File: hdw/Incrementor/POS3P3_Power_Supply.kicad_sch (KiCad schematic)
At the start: 13 parts, among them U301 TPS62130

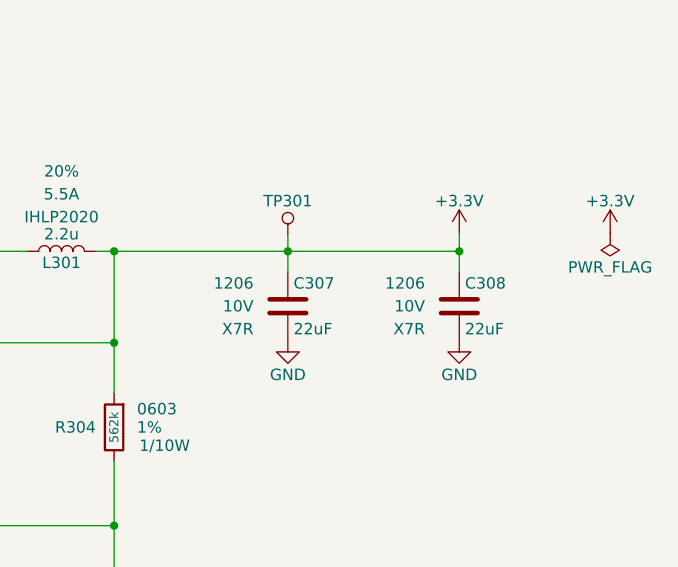
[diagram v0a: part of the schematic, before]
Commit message: renamed project, removed stuff I dont need
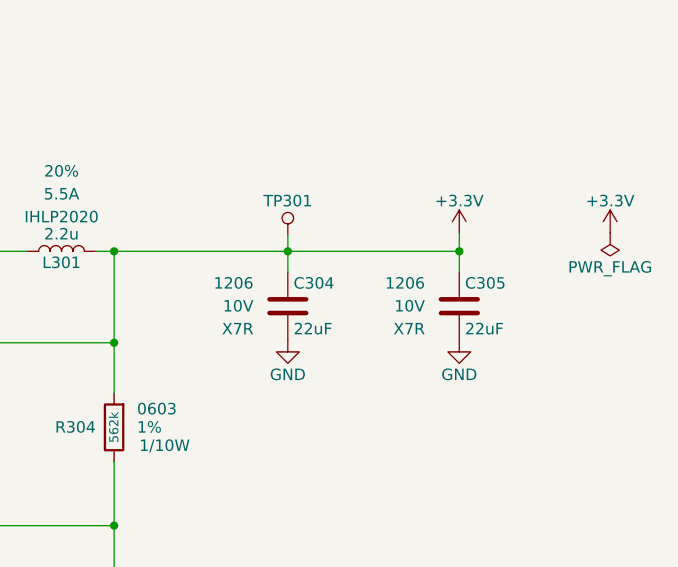
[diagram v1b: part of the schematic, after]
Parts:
- renumbered C307 to C304, C308 to C305
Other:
- company: (none) -> Drew Maatman
- title: QI Charger -> Stopwatch
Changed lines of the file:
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@@
   (paper "A")
   (title_block
-    (title "QI Charger")
-    (date "2019-01-03")
+    (title "Stopwatch")
+    (date "2024-01-02")
     (rev "A")
+    (company "Drew Maatman")
   )
   (junction (at 63.5 93.726) (diameter 0) (color 0 0 0 0)
@@
     (pin "2")
     (instances
-      (project "Incrementor"
+      (project "Stopwatch"
         (path "/c0d2575b-aec2-49ed-8c32-97fe6e68824c/00000000-0000-0000-0000-00005d779ae1"
           (reference "L301") (unit 1)
@@
   (symbol (lib_id "Custom_Library:C_Custom") (at 108.712 61.468 0) (unit 1)
     (in_bom yes) (on_board yes) (dnp no)
-    (property "Reference" "C?" (at 109.347 58.928 0)
+    (property "Reference" "C303" (at 109.347 58.928 0)
       (effects (font (size 1.27 1.27)) (justify left))
     )
@@
     (pin "2")
     (instances
-      (project "Incrementor"
+      (project "Stopwatch"
         (path "/c0d2575b-aec2-49ed-8c32-97fe6e68824c/00000000-0000-0000-0000-00005d779ae1"
           (reference "C303") (unit 1)
@@
     )
     (pin "1")
+    (instances
+      (project "Stopwatch"
+        (path "/c0d2575b-aec2-49ed-8c32-97fe6e68824c/00000000-0000-0000-0000-00005d779ae1"
+          (reference "#PWR0305") (unit 1)
+        )
+      )
+    )
   )
   (symbol (lib_id "Custom_Library:C_Custom") (at 63.5 61.468 0) (unit 1)
@@
     (pin "2")
     (instances
-      (project "Incrementor"
+      (project "Stopwatch"
         (path "/c0d2575b-aec2-49ed-8c32-97fe6e68824c/00000000-0000-0000-0000-00005d779ae1"
           (reference "C301") (unit 1)
@@
     )
     (pin "1")
+    (instances
+      (project "Stopwatch"
+        (path "/c0d2575b-aec2-49ed-8c32-97fe6e68824c/00000000-0000-0000-0000-00005d779ae1"
+          (reference "#PWR0302") (unit 1)
+        )
+      )
+    )
   )
   (symbol (lib_id "power:+12V") (at 63.5 51.054 0) (unit 1)
@@
     )
     (pin "1")
+    (instances
+      (project "Stopwatch"
+        (path "/c0d2575b-aec2-49ed-8c32-97fe6e68824c/00000000-0000-0000-0000-00005d779ae1"
+          (reference "#PWR0301") (unit 1)
+        )
+      )
+    )
   )
   (symbol (lib_id "Custom_Library:TPS62130") (at 130.048 81.026 0) (unit 1)
@@
     (pin "9")
     (instances
-      (project "Incrementor"
+      (project "Stopwatch"
         (path "/c0d2575b-aec2-49ed-8c32-97fe6e68824c/00000000-0000-0000-0000-00005d779ae1"
           (reference "U301") (unit 1)
@@
   (symbol (lib_id "Custom_Library:R_Custom") (at 86.36 61.468 0) (unit 1)
     (in_bom yes) (on_board yes) (dnp no)
-    (property "Reference" "R?" (at 84.328 61.468 0)
+    (property "Reference" "R302" (at 84.328 61.468 0)
       (effects (font (size 1.27 1.27)) (justify right))
     )
@@
     (pin "2")
     (instances
-      (project "Incrementor"
+      (project "Stopwatch"
         (path "/c0d2575b-aec2-49ed-8c32-97fe6e68824c/00000000-0000-0000-0000-00005d779ae1"
           (reference "R302") (unit 1)
@@
     )
     (pin "1")
+    (instances
+      (project "Stopwatch"
+        (path "/c0d2575b-aec2-49ed-8c32-97fe6e68824c/00000000-0000-0000-0000-00005d779ae1"
+          (reference "#PWR0303") (unit 1)
+        )
+      )
+    )
   )
   (symbol (lib_id "power:GND") (at 130.048 116.078 0) (unit 1)
@@
     )
     (pin "1")
+    (instances
+      (project "Stopwatch"
+        (path "/c0d2575b-aec2-49ed-8c32-97fe6e68824c/00000000-0000-0000-0000-00005d779ae1"
+          (reference "#PWR0307") (unit 1)
+        )
+      )
+    )
   )
   (symbol (lib_id "power:GND") (at 115.316 110.998 0) (unit 1)
@@
     )
     (pin "1")
+    (instances
+      (project "Stopwatch"
+        (path "/c0d2575b-aec2-49ed-8c32-97fe6e68824c/00000000-0000-0000-0000-00005d779ae1"
+          (reference "#PWR0306") (unit 1)
+        )
+      )
+    )
   )
   (symbol (lib_id "Custom_Library:C_Custom") (at 179.07 69.342 0) (unit 1)
     (in_bom yes) (on_board yes) (dnp no)
-    (property "Reference" "C307" (at 179.705 66.802 0)
+    (property "Reference" "C304" (at 179.705 66.802 0)
       (effects (font (size 1.27 1.27)) (justify left))
     )
@@
     (pin "2")
     (instances
-      (project "Incrementor"
+      (project "Stopwatch"
         (path "/c0d2575b-aec2-49ed-8c32-97fe6e68824c/00000000-0000-0000-0000-00005d779ae1"
           (reference "C304") (unit 1)
@@
   (symbol (lib_id "Custom_Library:R_Custom") (at 63.5 82.804 0) (unit 1)
     (in_bom yes) (on_board yes) (dnp no)
-    (property "Reference" "R?" (at 61.468 82.804 0)
+    (property "Reference" "R301" (at 61.468 82.804 0)
       (effects (font (size 1.27 1.27)) (justify right))
     )
@@
     (pin "2")
     (instances
-      (project "Incrementor"
+      (project "Stopwatch"
         (path "/c0d2575b-aec2-49ed-8c32-97fe6e68824c/00000000-0000-0000-0000-00005d779ae1"
           (reference "R301") (unit 1)
@@
   (symbol (lib_id "Custom_Library:C_Custom") (at 99.568 107.188 0) (unit 1)
     (in_bom yes) (on_board yes) (dnp no)
-    (property "Reference" "C?" (at 100.203 104.648 0)
+    (property "Reference" "C302" (at 100.203 104.648 0)
       (effects (font (size 1.27 1.27)) (justify left))
     )
@@
     (pin "2")
     (instances
-      (project "Incrementor"
+      (project "Stopwatch"
         (path "/c0d2575b-aec2-49ed-8c32-97fe6e68824c/00000000-0000-0000-0000-00005d779ae1"
           (reference "C302") (unit 1)
@@
     )
     (pin "1")
+    (instances
+      (project "Stopwatch"
+        (path "/c0d2575b-aec2-49ed-8c32-97fe6e68824c/00000000-0000-0000-0000-00005d779ae1"
+          (reference "#PWR0304") (unit 1)
+        )
+      )
+    )
   )
   (symbol (lib_id "Custom_Library:R_Custom") (at 159.766 82.804 0) (unit 1)
     (in_bom yes) (on_board yes) (dnp no)
-    (property "Reference" "R?" (at 157.734 82.804 0)
+    (property "Reference" "R304" (at 157.734 82.804 0)
       (effects (font (size 1.27 1.27)) (justify right))
     )
@@
     (pin "2")
     (instances
-      (project "Incrementor"
+      (project "Stopwatch"
         (path "/c0d2575b-aec2-49ed-8c32-97fe6e68824c/00000000-0000-0000-0000-00005d779ae1"
           (reference "R304") (unit 1)
@@
   (symbol (lib_id "Custom_Library:R_Custom") (at 159.766 105.918 0) (unit 1)
     (in_bom yes) (on_board yes) (dnp no)
-    (property "Reference" "R?" (at 157.734 105.918 0)
+    (property "Reference" "R305" (at 157.734 105.918 0)
       (effects (font (size 1.27 1.27)) (justify right))
     )
@@
     (pin "2")
     (instances
-      (project "Incrementor"
+      (project "Stopwatch"
         (path "/c0d2575b-aec2-49ed-8c32-97fe6e68824c/00000000-0000-0000-0000-00005d779ae1"
           (reference "R305") (unit 1)
@@
     )
     (pin "1")
+    (instances
+      (project "Stopwatch"
+        (path "/c0d2575b-aec2-49ed-8c32-97fe6e68824c/00000000-0000-0000-0000-00005d779ae1"
+          (reference "#PWR0308") (unit 1)
+        )
+      )
+    )
   )
   (symbol (lib_id "power:GND") (at 179.07 73.152 0) (unit 1)
@@
     )
     (pin "1")
+    (instances
+      (project "Stopwatch"
+        (path "/c0d2575b-aec2-49ed-8c32-97fe6e68824c/00000000-0000-0000-0000-00005d779ae1"
+          (reference "#PWR0309") (unit 1)
+        )
+      )
+    )
   )
   (symbol (lib_id "Custom_Library:C_Custom") (at 198.12 69.342 0) (unit 1)
     (in_bom yes) (on_board yes) (dnp no)
-    (property "Reference" "C308" (at 198.755 66.802 0)
+    (property "Reference" "C305" (at 198.755 66.802 0)
       (effects (font (size 1.27 1.27)) (justify left))
     )
@@
     (pin "2")
     (instances
-      (project "Incrementor"
+      (project "Stopwatch"
         (path "/c0d2575b-aec2-49ed-8c32-97fe6e68824c/00000000-0000-0000-0000-00005d779ae1"
           (reference "C305") (unit 1)
@@
     )
     (pin "1")
+    (instances
+      (project "Stopwatch"
+        (path "/c0d2575b-aec2-49ed-8c32-97fe6e68824c/00000000-0000-0000-0000-00005d779ae1"
+          (reference "#PWR0310") (unit 1)
+        )
+      )
+    )
   )
   (symbol (lib_id "Custom_Library:R_Custom") (at 86.36 82.804 0) (unit 1)
     (in_bom yes) (on_board yes) (dnp no)
-    (property "Reference" "R?" (at 84.328 82.804 0)
+    (property "Reference" "R303" (at 84.328 82.804 0)
       (effects (font (size 1.27 1.27)) (justify right))
     )
@@
     (pin "2")
     (instances
-      (project "Incrementor"
+      (project "Stopwatch"
         (path "/c0d2575b-aec2-49ed-8c32-97fe6e68824c/00000000-0000-0000-0000-00005d779ae1"
           (reference "R303") (unit 1)
@@
     (pin "1")
     (instances
-      (project "Incrementor"
+      (project "Stopwatch"
         (path "/c0d2575b-aec2-49ed-8c32-97fe6e68824c/00000000-0000-0000-0000-00005d779ae1"
           (reference "#FLG0301") (unit 1)
@@
   (symbol (lib_id "Custom_Library:TP") (at 179.07 61.468 0) (unit 1)
     (in_bom yes) (on_board yes) (dnp no)
-    (property "Reference" "TP?" (at 179.07 57.658 0)
+    (property "Reference" "TP301" (at 179.07 57.658 0)
       (effects (font (size 1.27 1.27)))
     )
@@
     (pin "1")
     (instances
-      (project "Incrementor"
+      (project "Stopwatch"
         (path "/c0d2575b-aec2-49ed-8c32-97fe6e68824c/00000000-0000-0000-0000-00005d779ae1"
           (reference "TP301") (unit 1)
@@
     )
     (pin "1")
+    (instances
+      (project "Stopwatch"
+        (path "/c0d2575b-aec2-49ed-8c32-97fe6e68824c/00000000-0000-0000-0000-00005d779ae1"
+          (reference "#PWR0101") (unit 1)
+        )
+      )
+    )
   )
   (symbol (lib_id "Incrementor-rescue:+3.3V-power") (at 214.884 61.214 0) (unit 1)
@@
     )
     (pin "1")
+    (instances
+      (project "Stopwatch"
+        (path "/c0d2575b-aec2-49ed-8c32-97fe6e68824c/00000000-0000-0000-0000-00005d779ae1"
+          (reference "#PWR0102") (unit 1)
+        )
+      )
+    )
   )
   (symbol (lib_id "Incrementor-rescue:+3.3V-power") (at 63.5 78.994 0) (unit 1)
@@
     )
     (pin "1")
+    (instances
+      (project "Stopwatch"
+        (path "/c0d2575b-aec2-49ed-8c32-97fe6e68824c/00000000-0000-0000-0000-00005d779ae1"
+          (reference "#PWR0103") (unit 1)
+        )
+      )
+    )
   )
 )
